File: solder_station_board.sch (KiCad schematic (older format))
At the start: 34 parts, among them J1 PWR_220V, J2 HEATER, J3 IO, J4 TEMP, J7 ROTARY, J8 SERIAL, P1 ISP, T1 Transformer_1P_2S, U1 MOC3020M, U2 LT1117-3.3, U3 PC817, U5 ATTINY2313-20SU

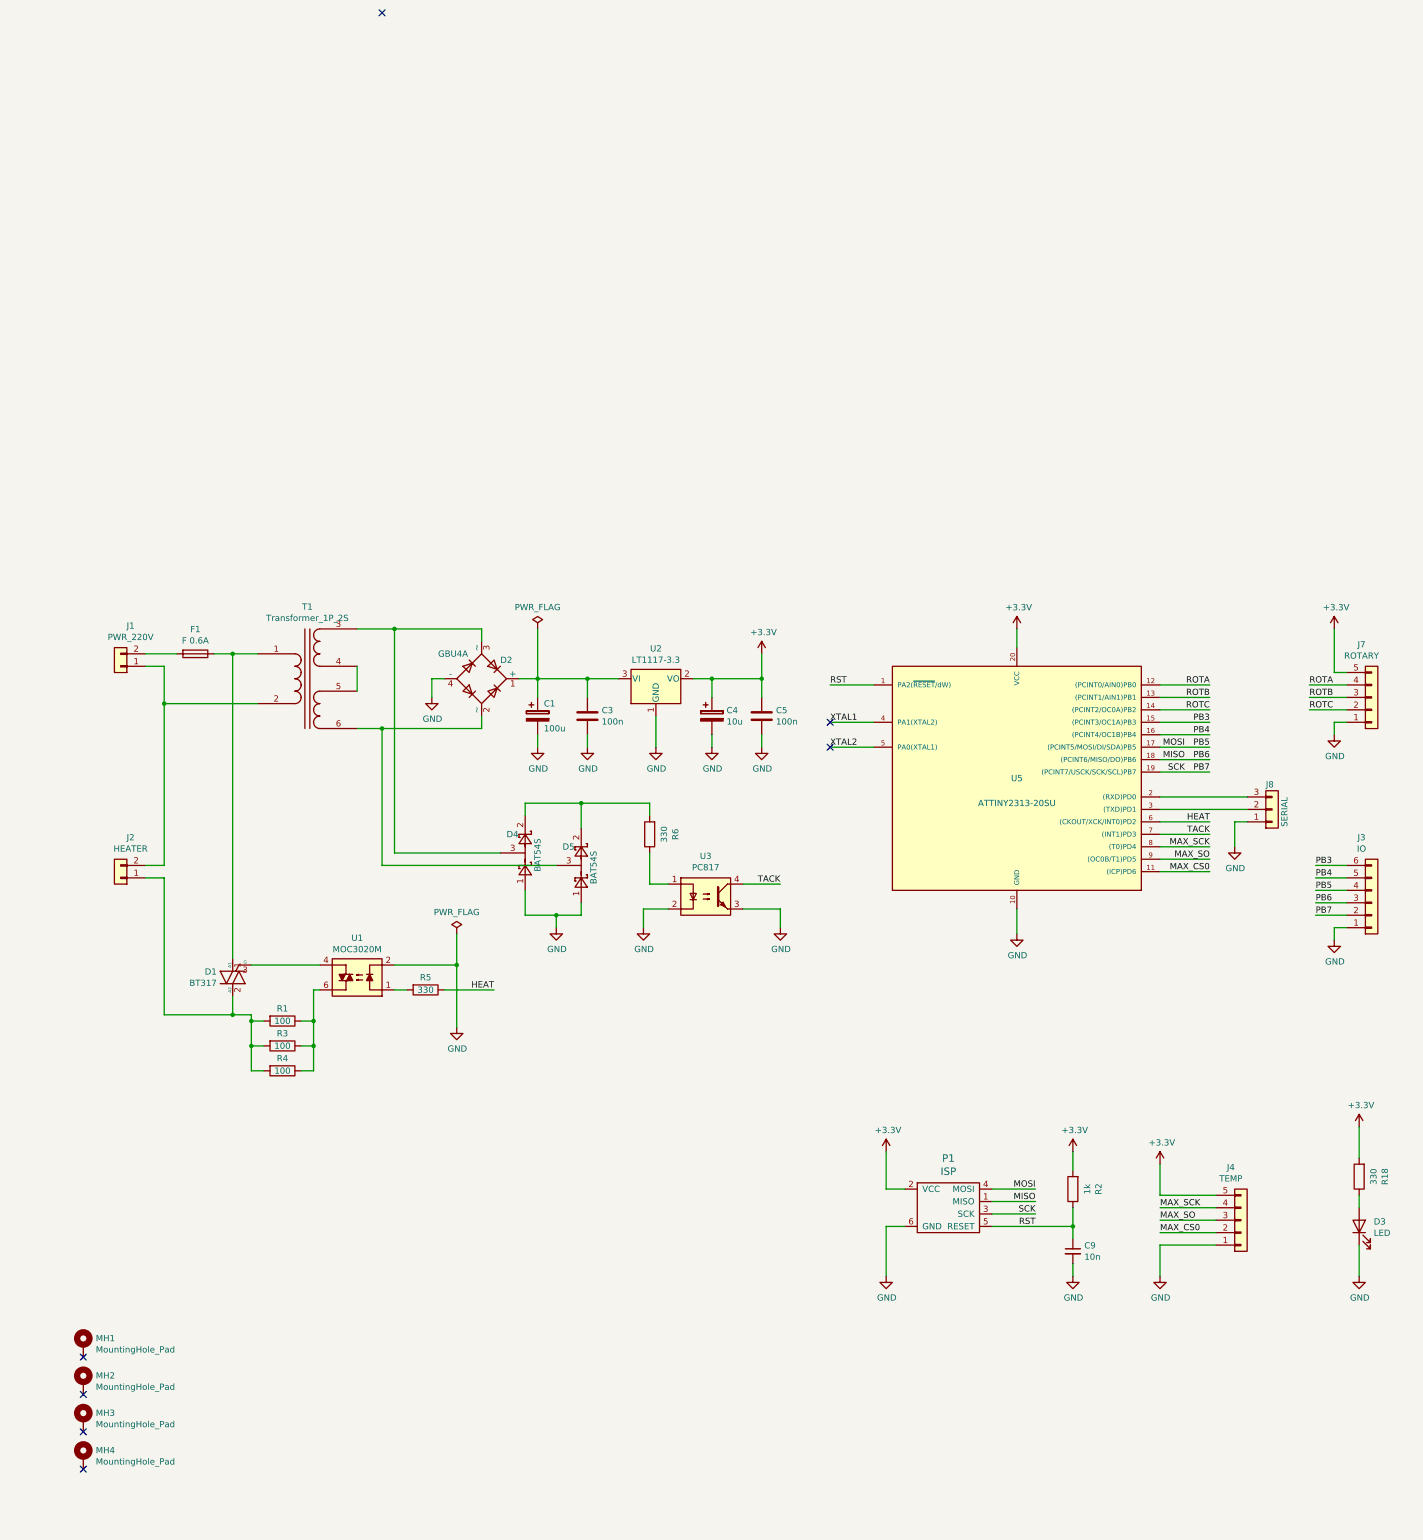
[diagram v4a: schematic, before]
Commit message: change bat to mb6s
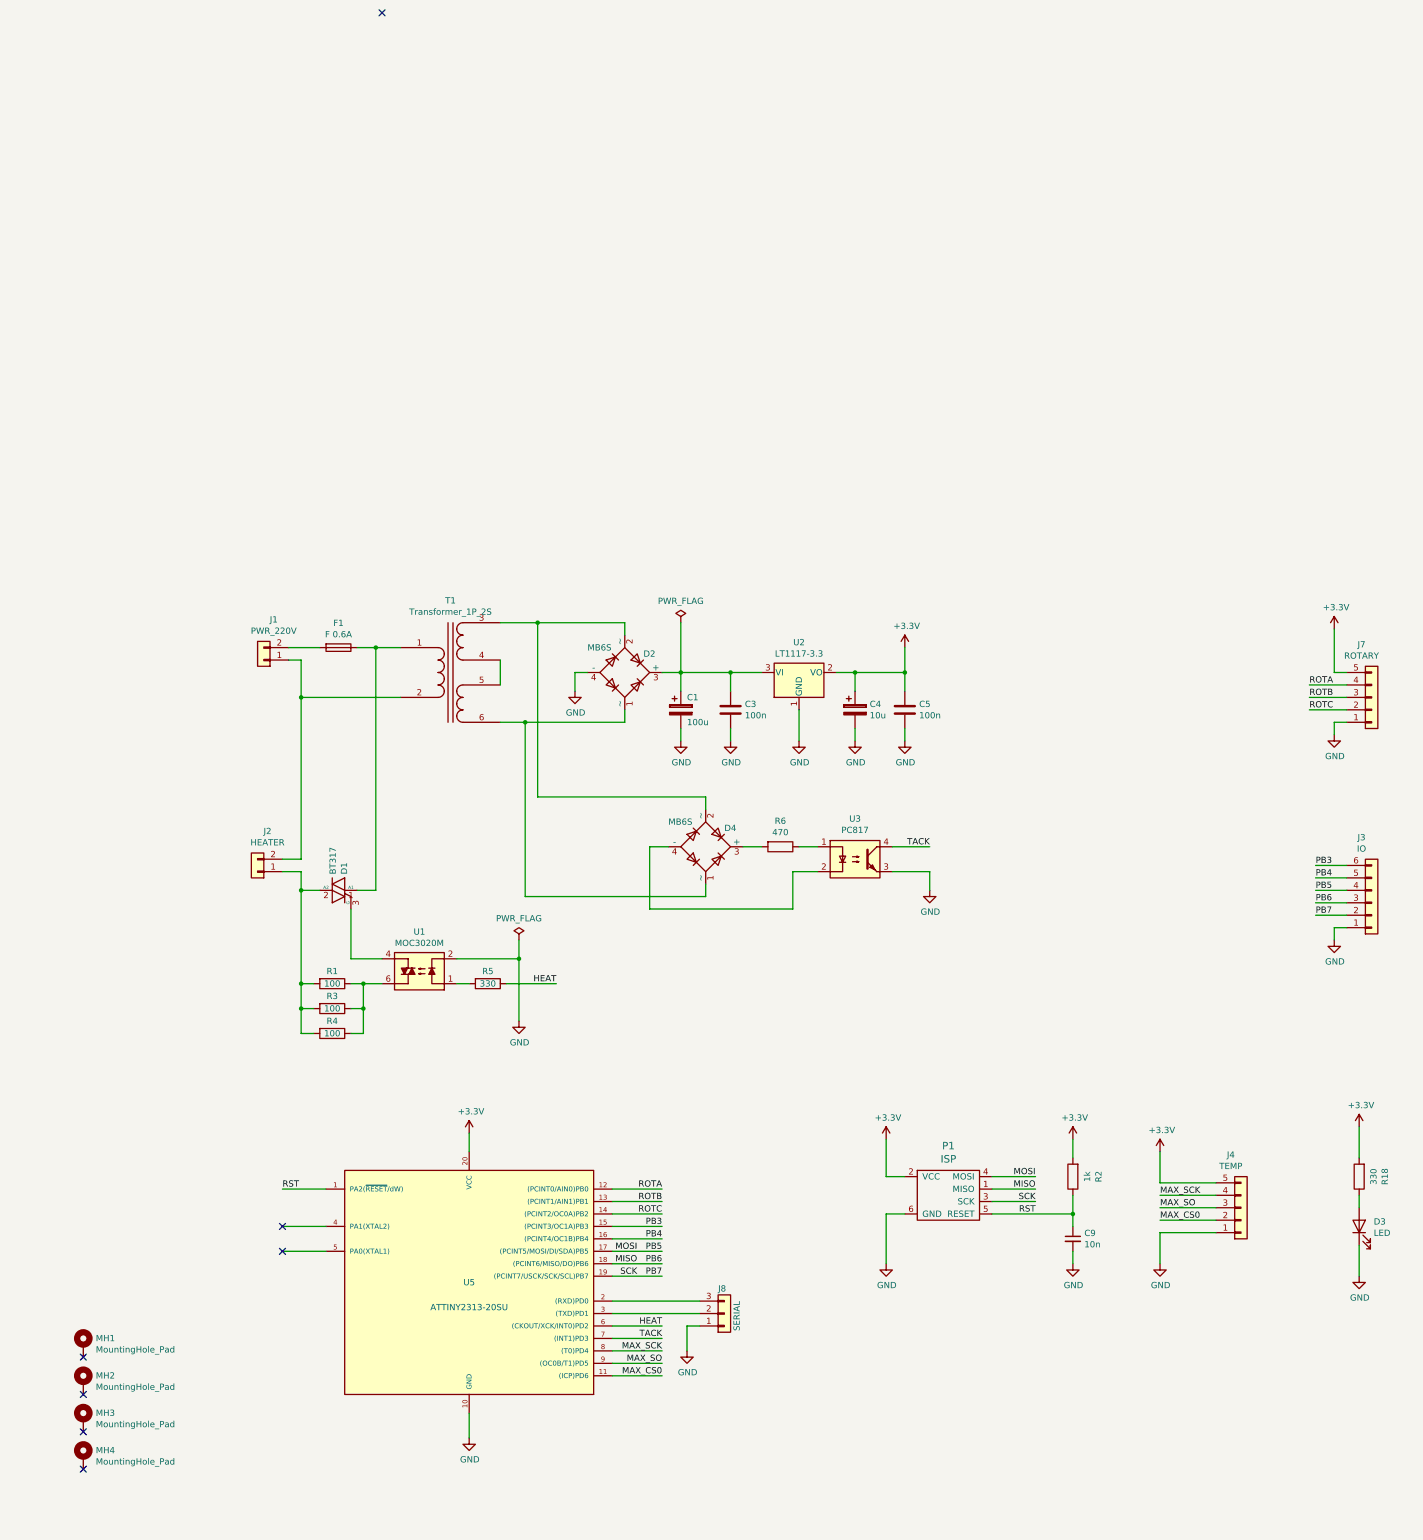
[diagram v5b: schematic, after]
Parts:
- removed D2: GBU4A, custom:Diode_Bridge_Vishay_GBU_20P3.8mm, symbol solder_station_board-rescue:GBU4A-Diode_Bridge
- removed D4, D5: BAT54S, Package_TO_SOT_SMD:SOT-23, symbol solder_station_board-rescue:BAT54S-Diode
- added D2, D4: MB6S, Package_TO_SOT_SMD:TO-269AA, symbol Diode_Bridge:MB6S
- J8: footprint Connector_PinHeader_2.54mm:PinHeader_1x03_P2.54mm_Vertical -> Connector_JST:JST_XH_B3B-XH-A_1x03_P2.50mm_Vertical
- R6: value 330 -> 470
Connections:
- net GND: now also D2.4 (-); no longer U3.2
- net at T1.3 (SA): now also D2.2 (~~), D4.2 (~~)
- net at T1.6 (SD): now also D2.1 (~~), D4.1 (~~)
- net at C1.1, C3.1, U2.3 (VI): now also D2.3 (+)
- net at R6.2: now also D4.3 (+)
- net XTAL1: no longer names the net of U5.4 (PA1(XTAL2))
- net XTAL2: no longer names the net of U5.5 (PA0(XTAL1))
- new net: D4.4 (-), U3.2
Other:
- moved on the sheet: C1, C3, C4, C5, C9, D1, F1, J1, J2, J4, J8, P1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
